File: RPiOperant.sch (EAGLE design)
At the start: 69 parts, among them IC1 74LS14N, IC2 74LS14N, J2 POWER_JACK

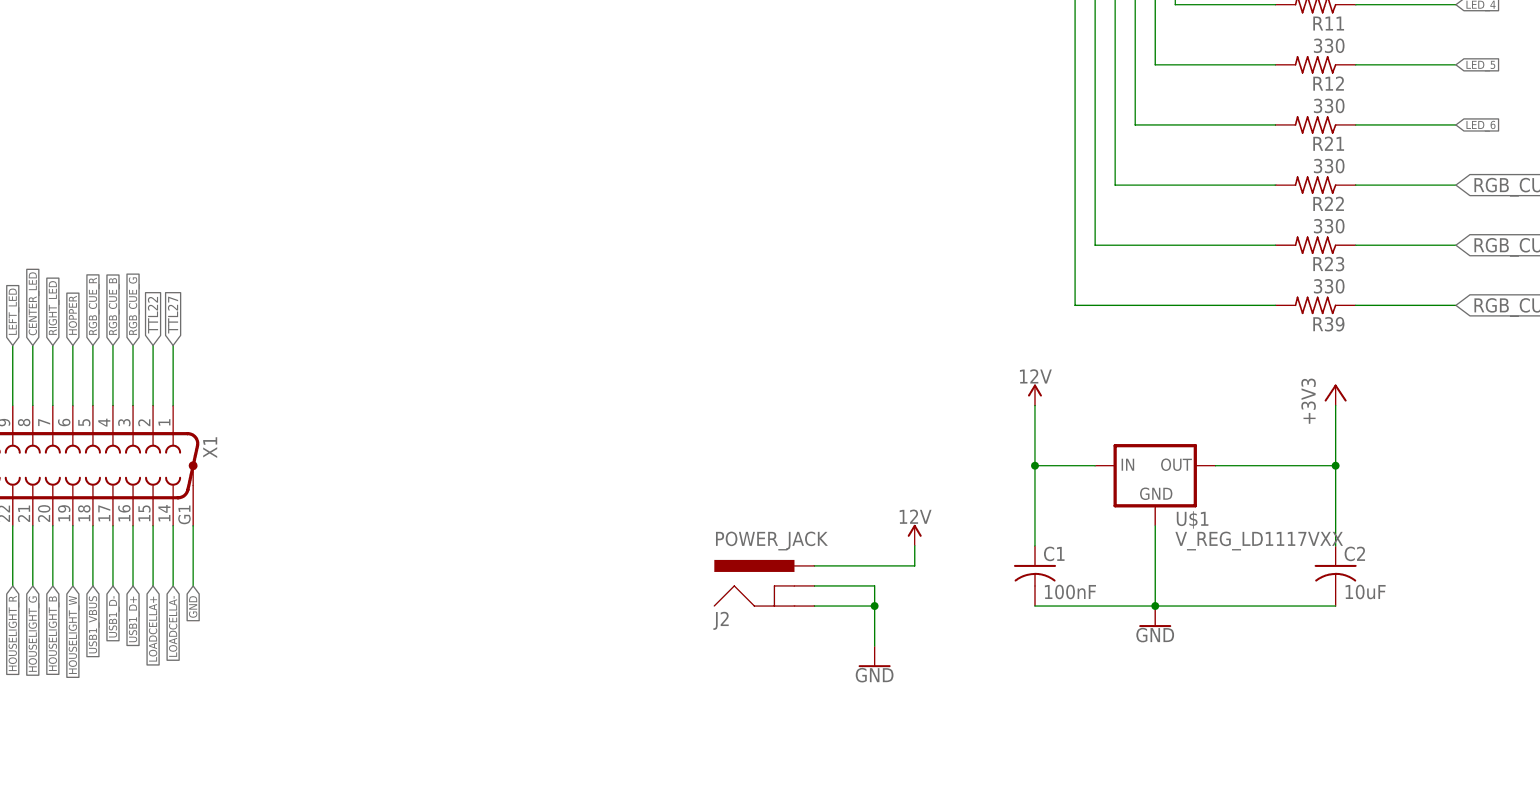
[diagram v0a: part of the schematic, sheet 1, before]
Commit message: rev b changes... new DB25 pinout
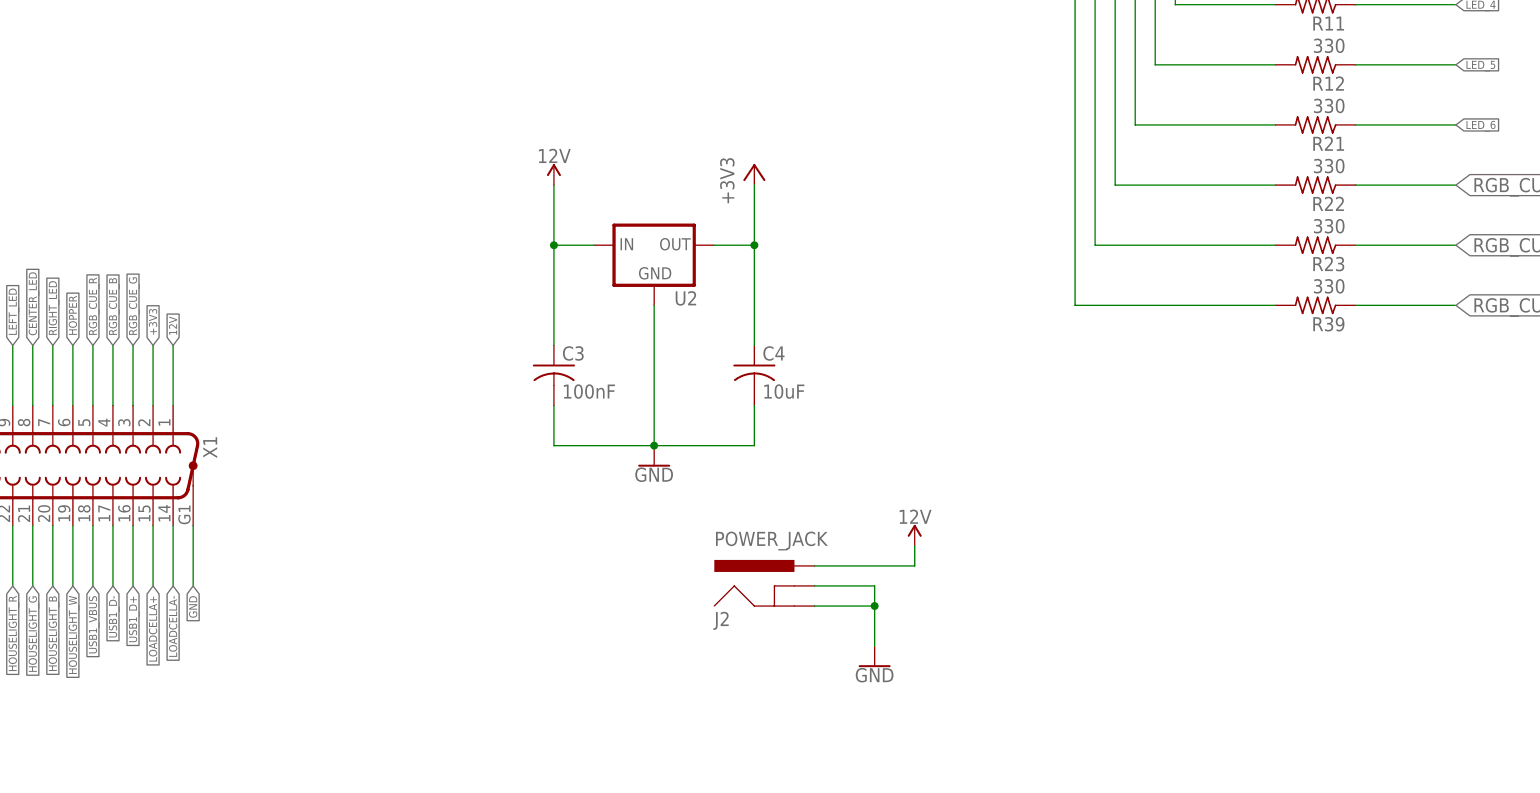
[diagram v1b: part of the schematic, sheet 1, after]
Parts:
- removed C1: 100nF, adafruit:C-US050-025X075
- removed C2: 10uF, adafruit:C-US050-025X075
- removed U$1: V_REG_LD1117VXX, SparkFun-IC-Power:V_REG_LD1117VXX
- added C3: 100nF, adafruit:C-US050-025X075
- added C4: 10uF, adafruit:C-US050-025X075
- added U2: (no value), SparkFun-IC-Power:V_REG_78XXSINK
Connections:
- net +3V3: now also C4.1, U2.OUT, X1.2; no longer C2.1, U$1.OUT
- net 12V: now also C3.1, U2.IN, X1.1; no longer C1.1, U$1.IN
- net GND: now also C3.2, C4.2, U2.GND; no longer C1.2, C2.2, U$1.GND
- net TTL22: no longer X1.2
- net TTL27: no longer X1.1
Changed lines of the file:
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@@
 <?xml version="1.0" encoding="utf-8"?>
 <!DOCTYPE eagle SYSTEM "eagle.dtd">
-<eagle version="8.4.1">
+<eagle version="8.4.3">
 <drawing>
 <settings>
@@
 <part name="J1" library="SparkFun-Connectors" deviceset="CONN_04" device="SCREW"/>
 <part name="SV3" library="con-lstb" library_urn="urn:adsk.eagle:library:162" deviceset="MA20-2" device="" package3d_urn="urn:adsk.eagle:package:8338/1"/>
-<part name="U$1" library="SparkFun-IC-Power" library_urn="urn:adsk.eagle:library:526" deviceset="V_REG_LD1117VXX" device="" package3d_urn="urn:adsk.eagle:package:39065/1"/>
-<part name="+3V7" library="supply1" library_urn="urn:adsk.eagle:library:371" deviceset="+3V3" device=""/>
-<part name="GND5" library="SparkFun-PowerSymbols" deviceset="GND" device=""/>
-<part name="C1" library="adafruit" deviceset="C-US" device="050-025X075" value="100nF"/>
-<part name="C2" library="adafruit" deviceset="C-US" device="050-025X075" value="10uF"/>
-<part name="SUPPLY1" library="SparkFun-PowerSymbols" deviceset="12V" device=""/>
+<part name="U2" library="SparkFun-IC-Power" deviceset="V_REG_78XX" device="SINK"/>
+<part name="C3" library="adafruit" deviceset="C-US" device="050-025X075" value="100nF"/>
+<part name="C4" library="adafruit" deviceset="C-US" device="050-025X075" value="10uF"/>
+<part name="GND6" library="SparkFun-PowerSymbols" deviceset="GND" device=""/>
+<part name="+3V1" library="supply1" library_urn="urn:adsk.eagle:library:371" deviceset="+3V3" device=""/>
+<part name="SUPPLY3" library="SparkFun-PowerSymbols" deviceset="12V" device=""/>
 </parts>
 <sheets>
@@
 <instance part="J1" gate="G$1" x="-139.7" y="208.28" rot="R270"/>
 <instance part="SV3" gate="G$1" x="-40.64" y="60.96" rot="R180"/>
-<instance part="U$1" gate="G$1" x="33.02" y="137.16"/>
-<instance part="+3V7" gate="G$1" x="55.88" y="147.32"/>
-<instance part="GND5" gate="1" x="33.02" y="116.84"/>
-<instance part="C1" gate="G$1" x="17.78" y="124.46"/>
-<instance part="C2" gate="G$1" x="55.88" y="124.46"/>
-<instance part="SUPPLY1" gate="G$1" x="17.78" y="144.78"/>
+<instance part="U2" gate="G$1" x="-30.48" y="165.1"/>
+<instance part="C3" gate="G$1" x="-43.18" y="149.86"/>
+<instance part="C4" gate="G$1" x="-17.78" y="149.86"/>
+<instance part="GND6" gate="1" x="-30.48" y="137.16"/>
+<instance part="+3V1" gate="G$1" x="-17.78" y="175.26"/>
+<instance part="SUPPLY3" gate="G$1" x="-43.18" y="172.72"/>
 </instances>
 <busses>
@@
 </segment>
 <segment>
-<pinref part="C1" gate="G$1" pin="2"/>
-<pinref part="GND5" gate="1" pin="GND"/>
-<wire x1="17.78" y1="119.38" x2="33.02" y2="119.38" width="0.1524" layer="91"/>
-<pinref part="C2" gate="G$1" pin="2"/>
-<wire x1="33.02" y1="119.38" x2="55.88" y2="119.38" width="0.1524" layer="91"/>
-<junction x="33.02" y="119.38"/>
-<pinref part="U$1" gate="G$1" pin="GND"/>
-<wire x1="33.02" y1="129.54" x2="33.02" y2="119.38" width="0.1524" layer="91"/>
+<pinref part="U2" gate="G$1" pin="GND"/>
+<pinref part="GND6" gate="1" pin="GND"/>
+<wire x1="-30.48" y1="157.48" x2="-30.48" y2="139.7" width="0.1524" layer="91"/>
+<pinref part="C3" gate="G$1" pin="2"/>
+<wire x1="-43.18" y1="144.78" x2="-43.18" y2="139.7" width="0.1524" layer="91"/>
+<wire x1="-43.18" y1="139.7" x2="-30.48" y2="139.7" width="0.1524" layer="91"/>
+<junction x="-30.48" y="139.7"/>
+<pinref part="C4" gate="G$1" pin="2"/>
+<wire x1="-17.78" y1="144.78" x2="-17.78" y2="139.7" width="0.1524" layer="91"/>
+<wire x1="-17.78" y1="139.7" x2="-30.48" y2="139.7" width="0.1524" layer="91"/>
 </segment>
 </net>
@@
 </segment>
 <segment>
-<pinref part="C1" gate="G$1" pin="1"/>
-<pinref part="U$1" gate="G$1" pin="IN"/>
-<wire x1="17.78" y1="127" x2="17.78" y2="137.16" width="0.1524" layer="91"/>
-<wire x1="17.78" y1="137.16" x2="25.4" y2="137.16" width="0.1524" layer="91"/>
-<wire x1="17.78" y1="144.78" x2="17.78" y2="137.16" width="0.1524" layer="91"/>
-<junction x="17.78" y="137.16"/>
-<pinref part="SUPPLY1" gate="G$1" pin="12V"/>
-</segment>
-<segment>
 <pinref part="X1" gate="G$1" pin="23"/>
 <wire x1="-114.3" y1="129.54" x2="-114.3" y2="121.92" width="0.1524" layer="91"/>
 <label x="-114.3" y="121.92" size="0.8128" layer="91" rot="R270" xref="yes"/>
+</segment>
+<segment>
+<pinref part="X1" gate="G$1" pin="1"/>
+<wire x1="-91.44" y1="144.78" x2="-91.44" y2="152.4" width="0.1524" layer="91"/>
+<label x="-91.44" y="152.4" size="1.016" layer="91" rot="R90" xref="yes"/>
+</segment>
+<segment>
+<pinref part="C3" gate="G$1" pin="1"/>
+<pinref part="U2" gate="G$1" pin="IN"/>
+<wire x1="-43.18" y1="152.4" x2="-43.18" y2="165.1" width="0.1524" layer="91"/>
+<wire x1="-43.18" y1="165.1" x2="-38.1" y2="165.1" width="0.1524" layer="91"/>
+<pinref part="SUPPLY3" gate="G$1" pin="12V"/>
+<wire x1="-43.18" y1="165.1" x2="-43.18" y2="172.72" width="0.1524" layer="91"/>
+<junction x="-43.18" y="165.1"/>
 </segment>
 </net>
@@
 </segment>
 <segment>
-<pinref part="U$1" gate="G$1" pin="OUT"/>
-<pinref part="C2" gate="G$1" pin="1"/>
-<wire x1="40.64" y1="137.16" x2="55.88" y2="137.16" width="0.1524" layer="91"/>
-<wire x1="55.88" y1="137.16" x2="55.88" y2="127" width="0.1524" layer="91"/>
-<pinref part="+3V7" gate="G$1" pin="+3V3"/>
-<wire x1="55.88" y1="144.78" x2="55.88" y2="137.16" width="0.1524" layer="91"/>
-<junction x="55.88" y="137.16"/>
+<pinref part="X1" gate="G$1" pin="2"/>
+<wire x1="-93.98" y1="144.78" x2="-93.98" y2="152.4" width="0.1524" layer="91"/>
+<label x="-93.98" y="152.4" size="1.016" layer="91" rot="R90" xref="yes"/>
+</segment>
+<segment>
+<pinref part="C4" gate="G$1" pin="1"/>
+<pinref part="U2" gate="G$1" pin="OUT"/>
+<wire x1="-17.78" y1="152.4" x2="-17.78" y2="165.1" width="0.1524" layer="91"/>
+<wire x1="-17.78" y1="165.1" x2="-22.86" y2="165.1" width="0.1524" layer="91"/>
+<pinref part="+3V1" gate="G$1" pin="+3V3"/>
+<wire x1="-17.78" y1="172.72" x2="-17.78" y2="165.1" width="0.1524" layer="91"/>
+<junction x="-17.78" y="165.1"/>
 </segment>
 </net>
@@
 <label x="114.3" y="350.52" size="1.778" layer="91" rot="R180" xref="yes"/>
 </segment>
-<segment>
-<pinref part="X1" gate="G$1" pin="1"/>
-<wire x1="-91.44" y1="144.78" x2="-91.44" y2="152.4" width="0.1524" layer="91"/>
-<label x="-91.44" y="152.4" size="1.27" layer="91" rot="R90" xref="yes"/>
-</segment>
 </net>
 <net name="TTL22" class="0">
@@
 <label x="139.7" y="116.84" size="1.778" layer="91" rot="R180" xref="yes"/>
 </segment>
-<segment>
-<pinref part="X1" gate="G$1" pin="2"/>
-<wire x1="-93.98" y1="144.78" x2="-93.98" y2="152.4" width="0.1524" layer="91"/>
-<label x="-93.98" y="152.4" size="1.27" layer="91" rot="R90" xref="yes"/>
-</segment>
-</net>
+</net>

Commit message: new board!
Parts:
- removed J1: (no value), SparkFun-Connectors:CONN_04SCREW
- removed J10, J13, J14: (no value), SparkFun-Connectors:CONN_03SCREW
- removed J15, J9: (no value), SparkFun-Connectors:CONN_023.5MM
- removed X2: (no value), con-subd:F25HP
- added X3: 2550-, con-3m:2550-
- X1: value (none) -> 2516-; device con-subd:F25HP -> con-3m:2516-
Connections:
- removed net N$32: J13.1, JP1.1
- removed net N$33: J13.2, JP4.1
- new net GPIO17EXT: JP1.1, X1-9.KL
- new net GPIO8EXT: JP4.1, X1-10.KL
- new net RGB_CUE_B\: X3-4.KL
- net +3V3: now also X3-2.KL; no longer X1.2
- net 12V: now also X3-1.KL, X3-23.KL; no longer X1.1, X1.23
- net AUX1: now also X1-1.KL, X3-26.KL; no longer J9.1, X2.1
- net AUX2: now also X1-2.KL, X3-27.KL; no longer J9.2, X2.2
- net AUX3: now also X1-3.KL, X3-28.KL; no longer J15.1, X2.3
- net AUX4: now also X1-4.KL, X3-29.KL; no longer J15.2, X2.4
- net AUX5: now also X1-5.KL, X3-30.KL; no longer J1.1, X2.5
- net AUX6: now also X1-6.KL, X3-31.KL; no longer J1.2, X2.6
- net AUX7: now also X1-7.KL, X3-32.KL; no longer J1.3, X2.7
- net AUX8: now also X1-8.KL, X3-39.KL; no longer J1.4, X2.14
- net CENTER_IR: now also X3-11.KL; no longer X1.11
- net CENTER_LED: now also X3-8.KL; no longer X1.8
- net GND: now also X1-15.KL, X1-16.KL; no longer J10.3, J13.3, J14.3, X1.G1, X1.G2, X2.G1, X2.G2
- net HOPPER: now also X3-6.KL; no longer X1.6
- net HOPPER_IR: now also X3-13.KL; no longer X1.13
- net HOUSELIGHT_B: now also X3-20.KL; no longer X1.20
- net HOUSELIGHT_G: now also X3-21.KL; no longer X1.21
- net HOUSELIGHT_R: now also X3-22.KL; no longer X1.22
- net HOUSELIGHT_W: now also X3-19.KL; no longer X1.19
- net IR_1: now also X3-50.KL; no longer X2.25
- net IR_2: now also X3-49.KL; no longer X2.24
- net IR_3: now also X3-48.KL; no longer X2.23
- net IR_4: now also X3-47.KL; no longer X2.22
- net IR_5: now also X3-46.KL; no longer X2.21
- net IR_6: now also X3-45.KL; no longer X2.20
- net LED_1: now also X3-38.KL; no longer X2.13
- net LED_2: now also X3-37.KL; no longer X2.12
- net LED_3: now also X3-36.KL; no longer X2.11
- net LED_4: now also X3-35.KL; no longer X2.10
- net LED_5: now also X3-34.KL; no longer X2.9
- net LED_6: now also X3-33.KL; no longer X2.8
- net LEFT_IR: now also X3-12.KL; no longer X1.12
- net LEFT_LED: now also X3-9.KL; no longer X1.9
- net LOADCELL2A+: now also X3-41.KL; no longer X2.16
- net LOADCELL2A-: now also X3-40.KL; no longer X2.15
- net LOADCELLA+: now also X3-15.KL; no longer X1.15
- net LOADCELLA-: now also X3-14.KL; no longer X1.14
- net LOADCELLE+: now also X3-25.KL; no longer X1.25
- net LOADCELLE-: now also X3-24.KL; no longer X1.24
- net RGB_CUE_B: no longer X1.4
- net RGB_CUE_G: now also X3-3.KL; no longer X1.3
- net RGB_CUE_R: now also X3-5.KL; no longer X1.5
- net RIGHT_IR: now also X3-10.KL; no longer X1.10
- net RIGHT_LED: now also X3-7.KL; no longer X1.7
- net RXD: now also X1-14.KL; no longer J14.2
- net TTL22: now also X1-12.KL; no longer J10.2
- net TTL27: now also X1-11.KL; no longer J10.1
- net TXD: now also X1-13.KL; no longer J14.1
- net USB1_D+: now also X3-16.KL; no longer X1.16
- net USB1_D-: now also X3-17.KL; no longer X1.17
- net USB1_VBUS: now also X3-18.KL; no longer X1.18
- net USB2_D+: now also X3-42.KL; no longer X2.17
- net USB2_D-: now also X3-43.KL; no longer X2.18
- net USB2_VBUS: now also X3-44.KL; no longer X2.19

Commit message: rev_b layout
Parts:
- added R18, R19: 330, resistor:R-US_0207/7
- added X2: 22-23-2041, con-molex:22-23-2041
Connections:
- new net N$25: R19.1, X2-2.S
- new net N$31: R18.1, X2-3.S
- net +3V3: now also R19.2
- net GND: now also X2-1.S, X2-4.S
- net RPI_3.3V: now also R18.2
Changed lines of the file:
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@@
 <part name="X3" library="con-3m" library_urn="urn:adsk.eagle:library:119" deviceset="2550-" device="" package3d_urn="urn:adsk.eagle:package:5594/1"/>
 <part name="X1" library="con-3m" library_urn="urn:adsk.eagle:library:119" deviceset="2516-" device="" package3d_urn="urn:adsk.eagle:package:5574/1"/>
+<part name="X2" library="con-molex" library_urn="urn:adsk.eagle:library:165" deviceset="22-23-2041" device=""/>
+<part name="GND5" library="SparkFun-PowerSymbols" deviceset="GND" device=""/>
+<part name="+3V7" library="supply1" library_urn="urn:adsk.eagle:library:371" deviceset="+3V3" device=""/>
+<part name="R18" library="resistor" library_urn="urn:adsk.eagle:library:348" deviceset="R-US_" device="0207/7" package3d_urn="urn:adsk.eagle:package:25942/1" value="330"/>
+<part name="R19" library="resistor" library_urn="urn:adsk.eagle:library:348" deviceset="R-US_" device="0207/7" package3d_urn="urn:adsk.eagle:package:25942/1" value="330"/>
 </parts>
 <sheets>
@@
 <instance part="X1" gate="-15" x="157.48" y="38.1"/>
 <instance part="X1" gate="-16" x="157.48" y="35.56"/>
+<instance part="X2" gate="-1" x="-91.44" y="167.64"/>
+<instance part="X2" gate="-2" x="-91.44" y="165.1"/>
+<instance part="X2" gate="-3" x="-91.44" y="162.56"/>
+<instance part="X2" gate="-4" x="-91.44" y="160.02"/>
+<instance part="GND5" gate="1" x="-101.6" y="149.86"/>
+<instance part="+3V7" gate="G$1" x="-127" y="182.88"/>
+<instance part="R18" gate="G$1" x="-119.38" y="162.56" rot="R180"/>
+<instance part="R19" gate="G$1" x="-119.38" y="170.18" rot="R180"/>
 </instances>
 <busses>
@@
 <label x="167.64" y="35.56" size="1.27" layer="91" xref="yes"/>
 </segment>
+<segment>
+<pinref part="X2" gate="-4" pin="S"/>
+<pinref part="GND5" gate="1" pin="GND"/>
+<wire x1="-93.98" y1="160.02" x2="-101.6" y2="160.02" width="0.1524" layer="91"/>
+<wire x1="-101.6" y1="160.02" x2="-101.6" y2="152.4" width="0.1524" layer="91"/>
+<pinref part="X2" gate="-1" pin="S"/>
+<wire x1="-93.98" y1="167.64" x2="-101.6" y2="167.64" width="0.1524" layer="91"/>
+<wire x1="-101.6" y1="167.64" x2="-101.6" y2="160.02" width="0.1524" layer="91"/>
+<junction x="-101.6" y="160.02"/>
+</segment>
 </net>
 <net name="12V" class="1">
@@
 <label x="-198.12" y="162.56" size="1.27" layer="91" xref="yes"/>
 </segment>
+<segment>
+<pinref part="+3V7" gate="G$1" pin="+3V3"/>
+<wire x1="-127" y1="180.34" x2="-127" y2="170.18" width="0.1524" layer="91"/>
+<pinref part="R19" gate="G$1" pin="2"/>
+<wire x1="-127" y1="170.18" x2="-124.46" y2="170.18" width="0.1524" layer="91"/>
+</segment>
 </net>
 <net name="HOPPER_IR_GPIO" class="0">
@@
 <label x="-58.42" y="66.04" size="1.016" layer="91" rot="R180" xref="yes"/>
 </segment>
+<segment>
+<pinref part="R18" gate="G$1" pin="2"/>
+<wire x1="-124.46" y1="162.56" x2="-134.62" y2="162.56" width="0.1524" layer="91"/>
+<wire x1="-134.62" y1="162.56" x2="-134.62" y2="180.34" width="0.1524" layer="91"/>
+<label x="-134.62" y="180.34" size="1.778" layer="91" rot="R90" xref="yes"/>
+</segment>
 </net>
 <net name="LOADCELLE+" class="0">
@@
 </segment>
 </net>
+<net name="N$25" class="0">
+<segment>
+<pinref part="R19" gate="G$1" pin="1"/>
+<wire x1="-114.3" y1="170.18" x2="-111.76" y2="170.18" width="0.1524" layer="91"/>
+<wire x1="-111.76" y1="170.18" x2="-111.76" y2="165.1" width="0.1524" layer="91"/>
+<pinref part="X2" gate="-2" pin="S"/>
+<wire x1="-111.76" y1="165.1" x2="-93.98" y2="165.1" width="0.1524" layer="91"/>
+</segment>
+</net>
+<net name="N$31" class="0">
+<segment>
+<pinref part="R18" gate="G$1" pin="1"/>
+<pinref part="X2" gate="-3" pin="S"/>
+<wire x1="-114.3" y1="162.56" x2="-93.98" y2="162.56" width="0.1524" layer="91"/>
+</segment>
+</net>

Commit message: revb
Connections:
- removed net CENTNER_LED: R36.1
- removed net RGB_CUE_B\: X3-4.KL
- net CENTER_LED: now also R36.1
- net RGB_CUE_B: now also X3-4.KL
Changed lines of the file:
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@@
 <label x="-198.12" y="154.94" size="1.27" layer="91" xref="yes"/>
+</segment>
+<segment>
+<pinref part="R36" gate="G$1" pin="1"/>
+<wire x1="58.42" y1="233.68" x2="71.12" y2="233.68" width="0.1524" layer="91"/>
+<label x="71.12" y="233.68" size="1.778" layer="91" xref="yes"/>
 </segment>
 </net>
@@
 <label x="71.12" y="157.48" size="1.778" layer="91" xref="yes"/>
 </segment>
+<segment>
+<pinref part="X3" gate="-4" pin="KL"/>
+<wire x1="-200.66" y1="160.02" x2="-198.12" y2="160.02" width="0.1524" layer="91"/>
+<label x="-198.12" y="160.02" size="1.016" layer="91" xref="yes"/>
+</segment>
 </net>
 <net name="RGB_CUE_G" class="0">
@@
 <wire x1="-200.66" y1="147.32" x2="-198.12" y2="147.32" width="0.1524" layer="91"/>
 <label x="-198.12" y="147.32" size="1.27" layer="91" xref="yes"/>
-</segment>
-</net>
-<net name="CENTNER_LED" class="0">
-<segment>
-<pinref part="R36" gate="G$1" pin="1"/>
-<wire x1="58.42" y1="233.68" x2="71.12" y2="233.68" width="0.1524" layer="91"/>
-<label x="71.12" y="233.68" size="1.016" layer="91" xref="yes"/>
 </segment>
 </net>
@@
 </segment>
 </net>
-<net name="RGB_CUE_B\" class="0">
-<segment>
-<pinref part="X3" gate="-4" pin="KL"/>
-<wire x1="-200.66" y1="160.02" x2="-198.12" y2="160.02" width="0.1524" layer="91"/>
-<label x="-198.12" y="160.02" size="1.27" layer="91" xref="yes"/>
-</segment>
-</net>
